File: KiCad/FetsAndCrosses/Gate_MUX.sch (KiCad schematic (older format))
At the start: 0 parts

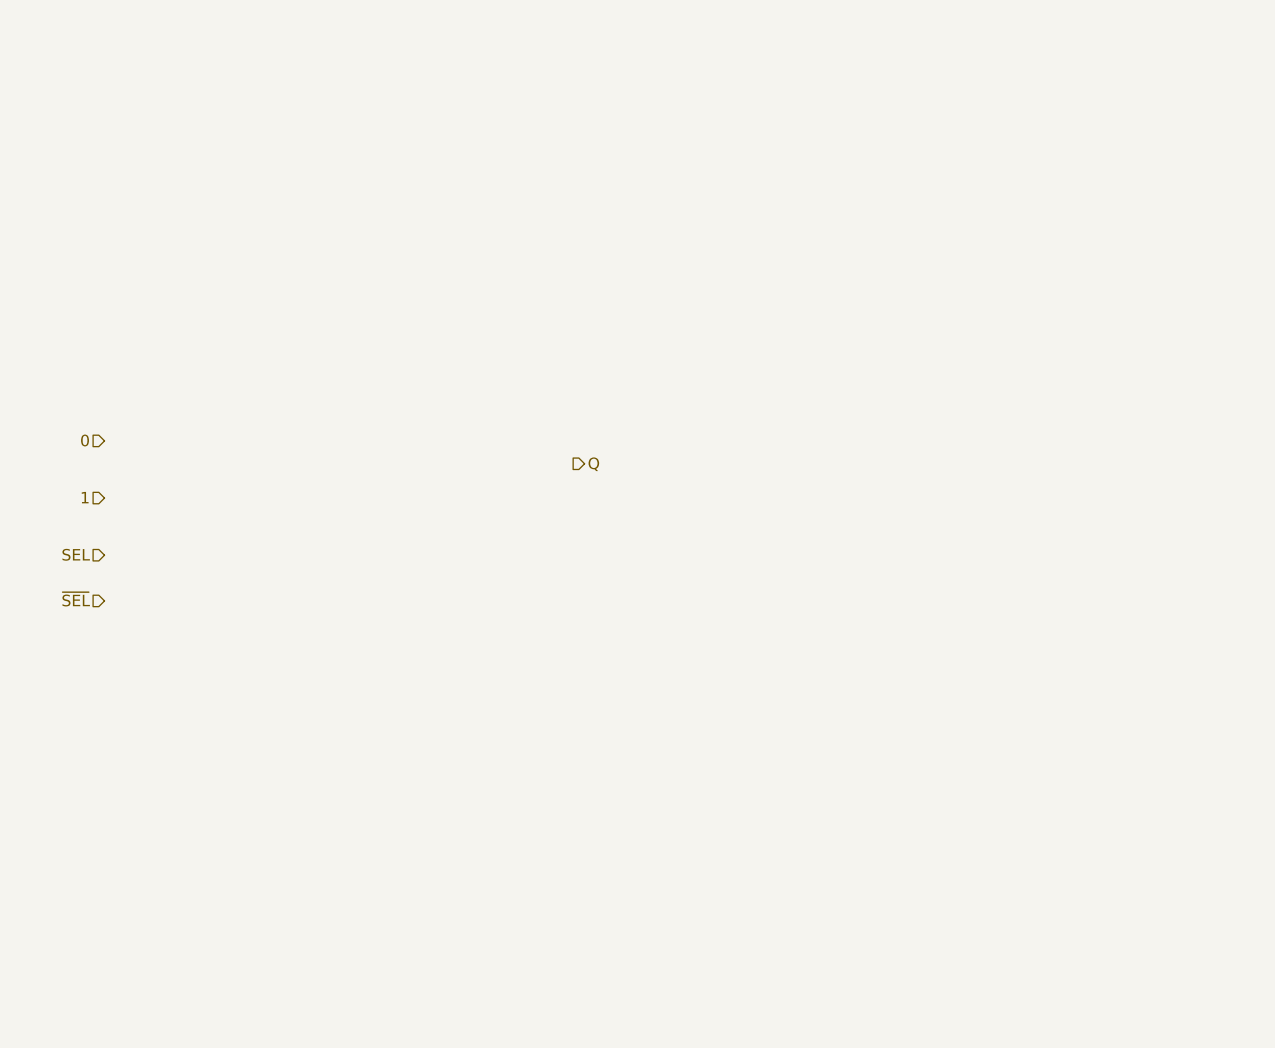
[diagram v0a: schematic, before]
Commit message: Reworked everything to use Buses
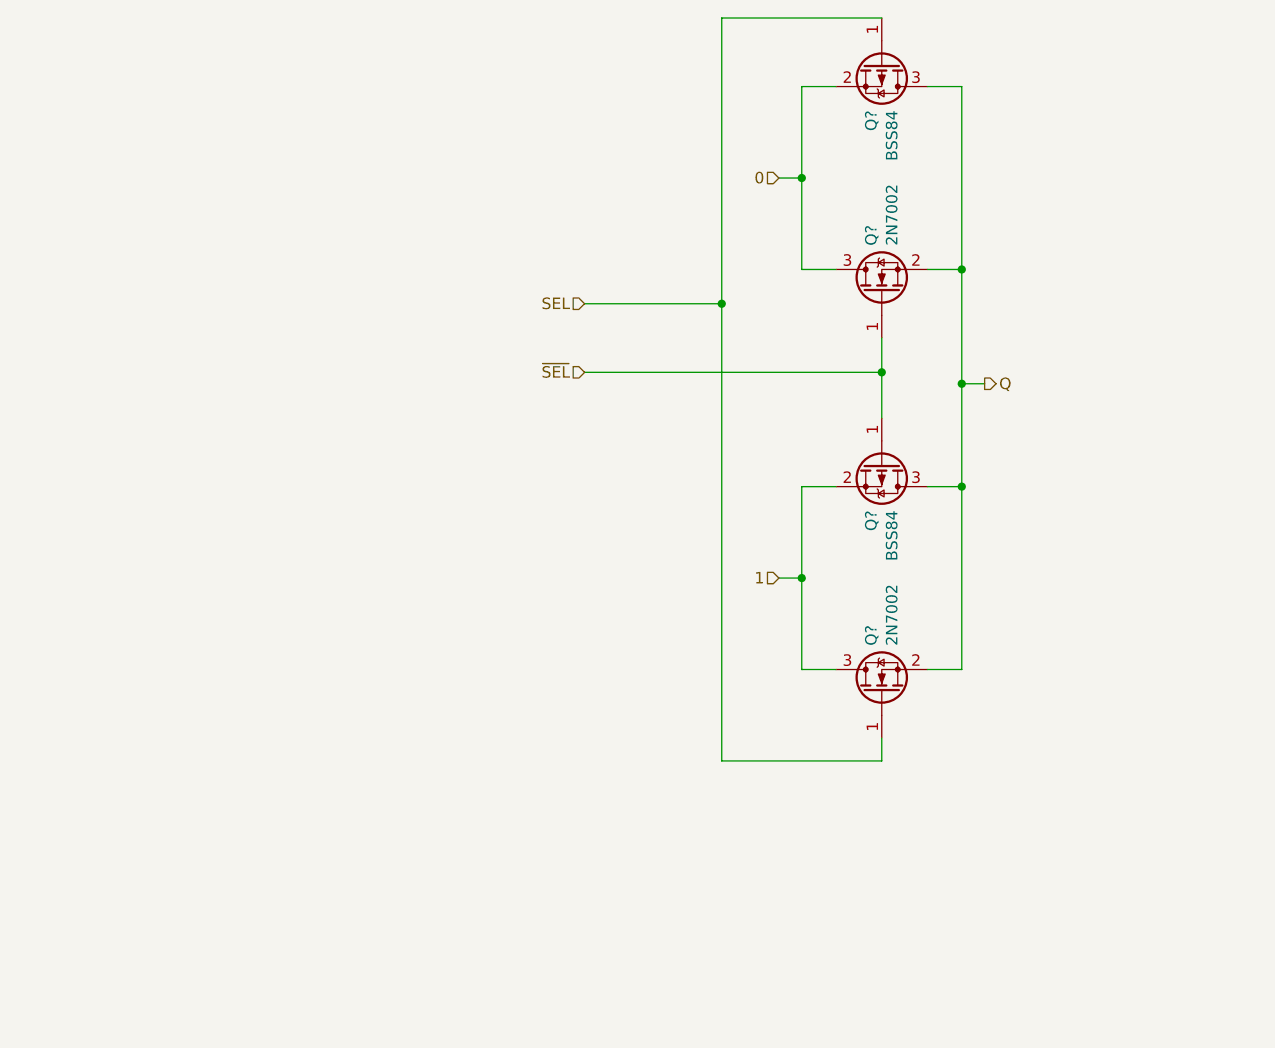
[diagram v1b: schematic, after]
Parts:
- added Q? (x2): BSS84, symbol Device:Q_PMOS_GSD
- added Q? (x2): 2N7002, symbol Device:Q_NMOS_GSD
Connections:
- net 0: now also Q?.2 (S), Q?.3 (D)
- net 1: now also Q?.2 (S), Q?.3 (D)
- net Q: now also Q?.2 (S), Q?.2 (S), Q?.3 (D), Q?.3 (D)
- net SEL: now also Q?.1 (G), Q?.1 (G)
- net ~SEL: now also Q?.1 (G), Q?.1 (G)

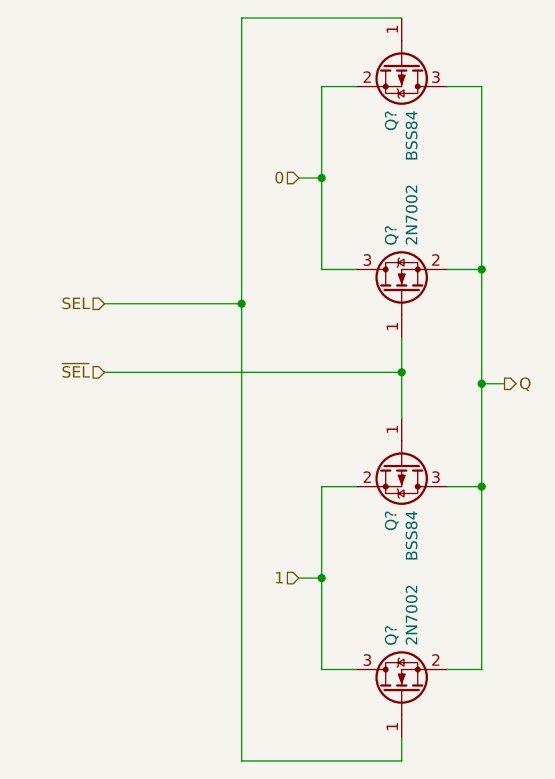
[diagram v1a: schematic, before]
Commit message: Schematic Done, Footprints assigned, ERC OK.
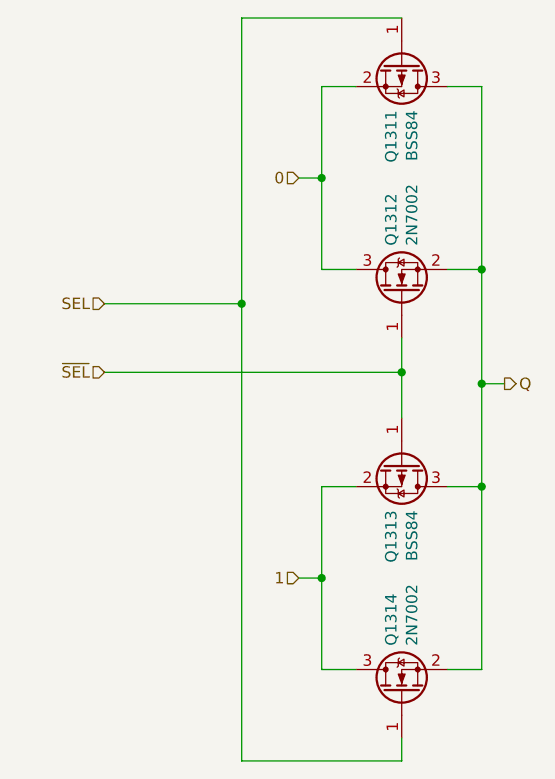
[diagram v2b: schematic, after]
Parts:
- Q407, Q409: renamed from Q?; footprint (none) -> LogicQ:SOT-23-P
- Q408, Q410: renamed from Q?; footprint (none) -> LogicQ:SOT-23-N

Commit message: Schematic fixes.
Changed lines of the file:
@@
 $Descr A4 11693 8268
 encoding utf-8
-Sheet 10 389
+Sheet 114 389
 Title ""
-Date ""
-Rev ""
-Comp ""
-Comment1 ""
+Date "2020-07-05"
+Rev "v0.0"
+Comp "Philipp Schilk"
+Comment1 "c"
 Comment2 ""
 Comment3 ""
@@
 AR Path="/5FB775FE/5F1827C2/5F172B02/5EF89D32" Ref="Q1269"  Part="1"
 AR Path="/5FB775FE/5F1827D4/5F172B02/5EF89D32" Ref="Q1311"  Part="1"
-F 0 "Q1311" H 6554 1454 50  0000 L CNN
+F 0 "Q383" H 6554 1454 50  0000 L CNN
 F 1 "BSS84" H 6554 1545 50  0000 L CNN
 F 2 "LogicQ:SOT-23-P" H 6550 1600 50  0001 C CNN
@@
 AR Path="/5FB775FE/5F1827C2/5F172B02/5EF89D38" Ref="Q1270"  Part="1"
 AR Path="/5FB775FE/5F1827D4/5F172B02/5EF89D38" Ref="Q1312"  Part="1"
-F 0 "Q1312" H 6554 2546 50  0000 L CNN
+F 0 "Q384" H 6554 2546 50  0000 L CNN
 F 1 "2N7002" H 6554 2455 50  0000 L CNN
 F 2 "LogicQ:SOT-23-N" H 6550 2600 50  0001 C CNN
@@
 AR Path="/5FB775FE/5F1827C2/5F172B02/5EF95E50" Ref="Q1271"  Part="1"
 AR Path="/5FB775FE/5F1827D4/5F172B02/5EF95E50" Ref="Q1313"  Part="1"
-F 0 "Q1313" H 6554 3204 50  0000 L CNN
+F 0 "Q385" H 6554 3204 50  0000 L CNN
 F 1 "BSS84" H 6554 3295 50  0000 L CNN
 F 2 "LogicQ:SOT-23-P" H 6550 3350 50  0001 C CNN
@@
 AR Path="/5FB775FE/5F1827C2/5F172B02/5EF95E56" Ref="Q1272"  Part="1"
 AR Path="/5FB775FE/5F1827D4/5F172B02/5EF95E56" Ref="Q1314"  Part="1"
-F 0 "Q1314" H 6554 4296 50  0000 L CNN
+F 0 "Q386" H 6554 4296 50  0000 L CNN
 F 1 "2N7002" H 6554 4205 50  0000 L CNN
 F 2 "LogicQ:SOT-23-N" H 6550 4350 50  0001 C CNN

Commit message: First Draft Schematic Updates
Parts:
- added Q1021, Q1023: BSS84, LogicQ:SOT-23-P, symbol Device:Q_PMOS_GSD
- added Q1022, Q1024: 2N7002, LogicQ:SOT-23-N, symbol Device:Q_NMOS_GSD
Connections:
- net 0: now also Q1023.1 (G), Q1024.1 (G); no longer Q407.2 (S), Q408.3 (D)
- net 1: now also Q1021.1 (G), Q1022.1 (G); no longer Q409.2 (S), Q410.3 (D)
- net Q: no longer Q407.3 (D), Q408.2 (S), Q409.3 (D), Q410.2 (S)
- net SEL: now also Q409.1 (G); no longer Q407.1 (G)
- net ~SEL: now also Q407.1 (G); no longer Q409.1 (G)
- new net: Q1021.3 (D), Q407.2 (S)
- new net: Q1024.3 (D), Q408.2 (S)
- new net: Q1023.3 (D), Q409.2 (S)
- new net: Q1022.3 (D), Q410.2 (S)
- new net +5V: Q1021.2 (S), Q1023.2 (S)
- new net GND: Q1022.2 (S), Q1024.2 (S)
- new net sheet5F4E3E19/A: Q407.3 (D), Q408.3 (D), Q409.3 (D), Q410.3 (D)
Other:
- note added: "!"
- moved on the sheet: Q415, Q416, Q417, Q418
